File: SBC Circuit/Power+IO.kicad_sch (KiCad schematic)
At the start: 40 parts, among them J1 USB_B, J2 Conn_01x02_Pin, J4 Conn_01x06_Pin, J8 Conn_01x02_Pin, J9 Conn_02x04_Odd_Even, Q1 AOI21357, Q2 AOI21357, U10 FT230XS, U8 LM7805_TO220, U9 LD1117AV33

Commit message: Wire phase done
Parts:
- TP2: value 3V TEST -> 3.3V TEST
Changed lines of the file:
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@@
   (title_block
     (title "POWER & IO")
-    (date "2024-01-26")
-    (rev "0.6")
+    (date "2024-01-31")
+    (rev "0.7")
     (company "LeTourneau University")
     (comment 1 "Richard Homan")
@@
       (effects (font (size 1.27 1.27)) (justify left))
     )
-    (property "Value" "3V TEST" (at 129.54 145.288 0)
-      (effects (font (size 1.27 1.27)) (justify left))
-    )
+    (property "Value" "3.3V TEST" (at 129.54 145.288 0)
+      (effects (font (size 1.27 1.27)) (justify left))
+    )

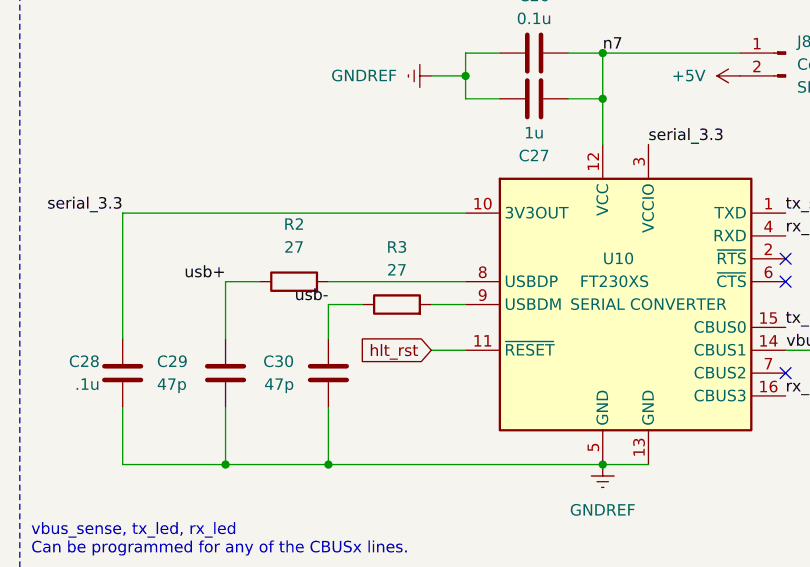
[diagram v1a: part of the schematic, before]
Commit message: All lines connected
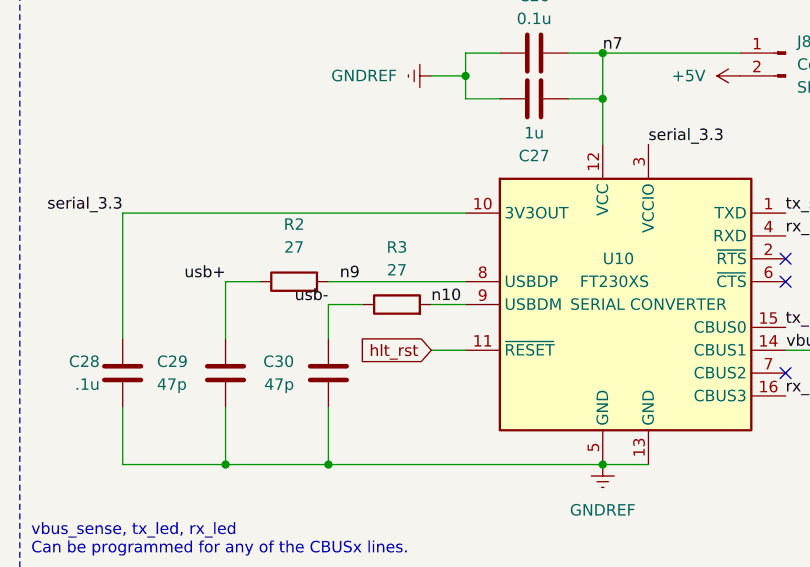
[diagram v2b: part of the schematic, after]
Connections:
- net n9: now reaches R2.2, U10.8 (USBDP)
- net n10: now reaches R3.2, U10.9 (USBDM)
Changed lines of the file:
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@@
     (effects (font (size 1.27 1.27)) (justify right bottom))
+  )
+  (label "n9" (at 54.61 62.23 0) (fields_autoplaced)
+    (effects (font (size 1.27 1.27)) (justify left bottom))
+    (property "Netclass" "signal" (at 54.61 63.5 0)
+      (effects (font (size 1.27 1.27) italic) (justify left) hide)
+    )
   )
   (label "tx_s" (at 250.19 130.81 0) (fields_autoplaced)
@@
     )
   )
+  (label "n10" (at 64.77 64.77 0) (fields_autoplaced)
+    (effects (font (size 1.27 1.27)) (justify left bottom))
+    (property "Netclass" "signal" (at 64.77 66.04 0)
+      (effects (font (size 1.27 1.27) italic) (justify left) hide)
+    )
+  )

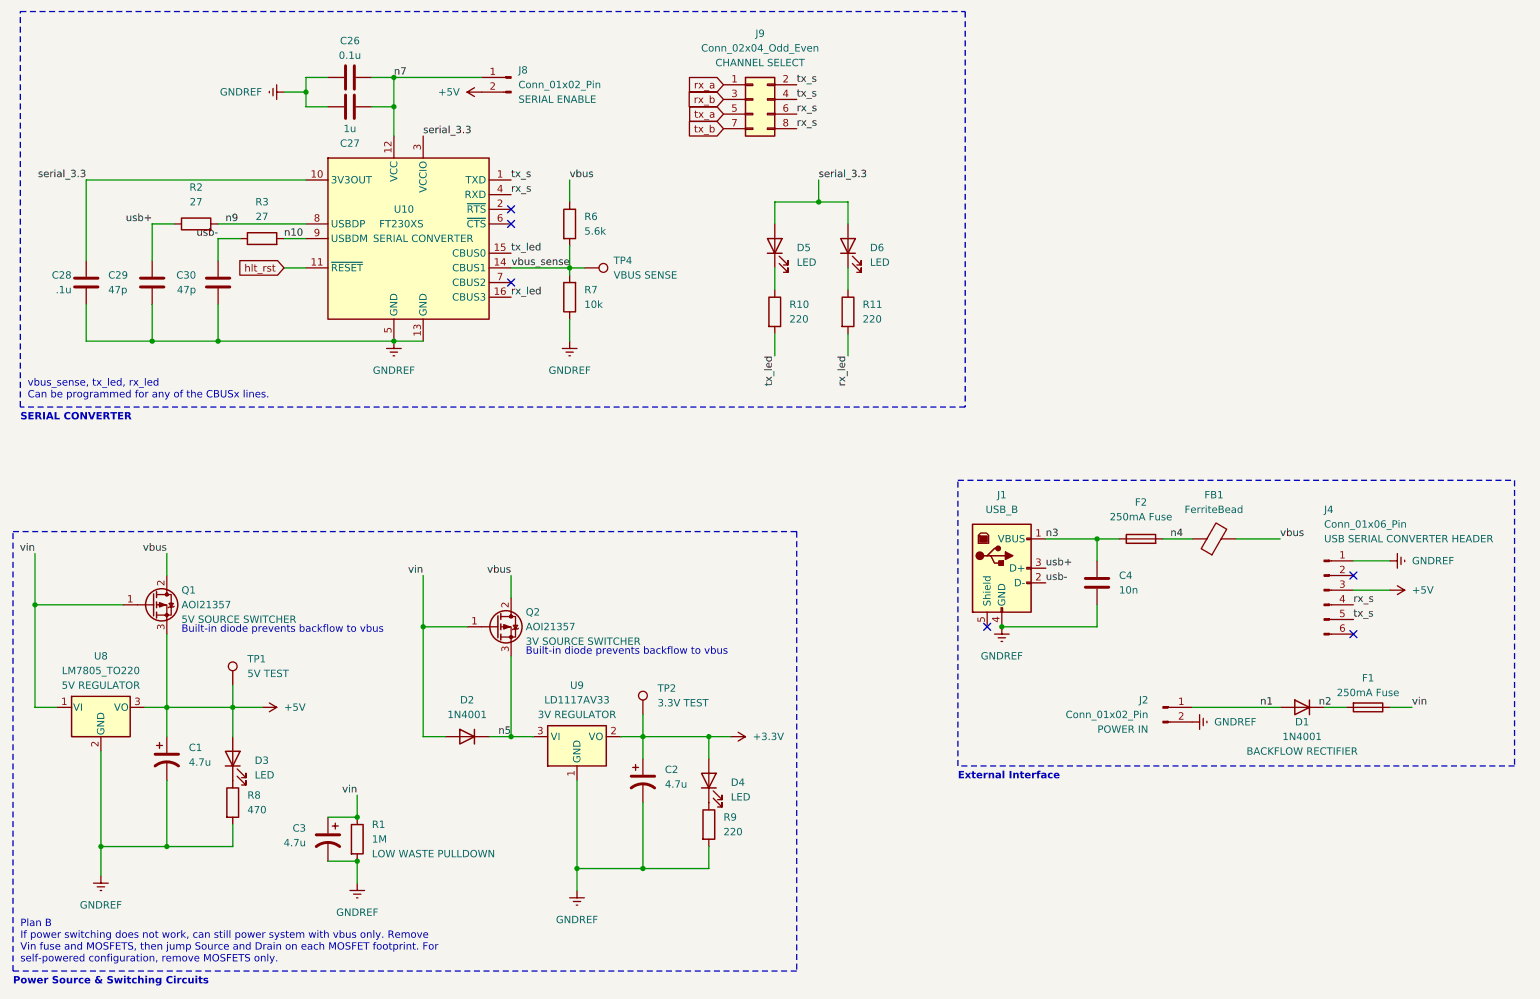
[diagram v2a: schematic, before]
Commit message: Add ground test point
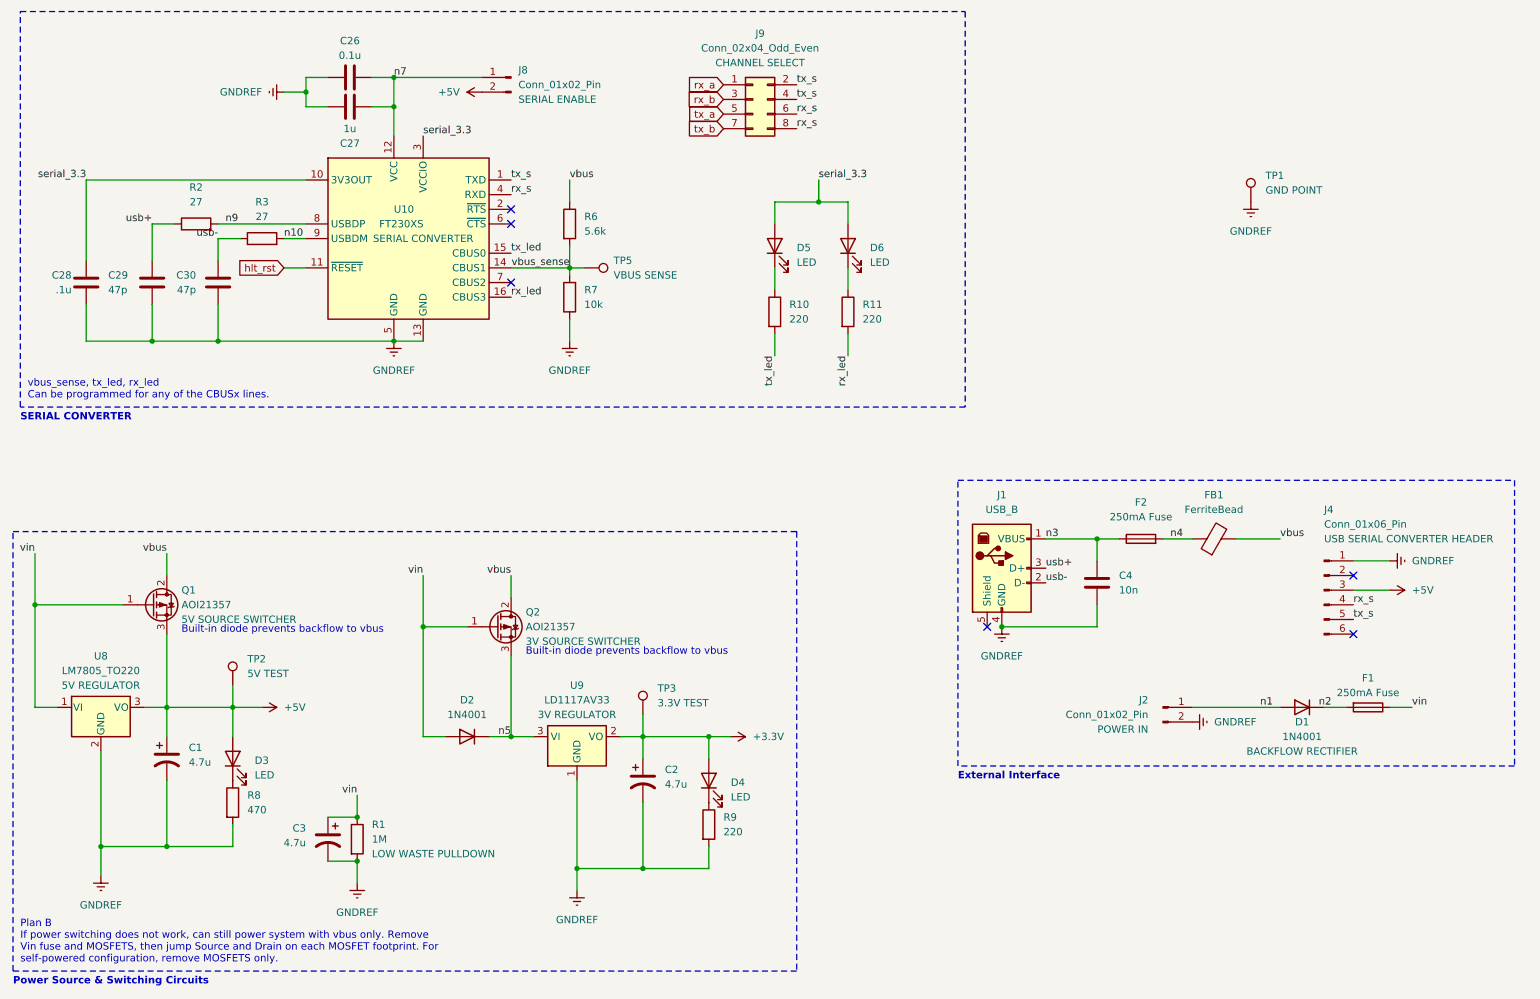
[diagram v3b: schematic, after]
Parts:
- added TP1: GND POINT, TestPoint:TestPoint_Keystone_5000-5004_Miniature, symbol Connector:TestPoint
- renumbered TP1 to TP2, TP2 to TP3, TP4 to TP5
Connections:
- net GNDREF: now also TP1.1

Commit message: Update schematic and PCB for requested changes
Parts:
- renumbered C26 to C30, C27 to C31, C28 to C32, C29 to C33, C30 to C34, R9 to R10, R10 to R11, R11 to R12, R6 to R7, R7 to R8, R8 to R9
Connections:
- net hlt_rst renamed rst
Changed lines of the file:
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@@
   (title_block
     (title "POWER & IO")
-    (date "2024-02-04")
-    (rev "0.8")
+    (date "2024-02-07")
+    (rev "0.9")
     (company "LeTourneau University")
     (comment 1 "Richard Homan")
@@
     )
   )
-  (global_label "hlt_rst" (shape input) (at 64.77 69.85 180) (fields_autoplaced)
+  (global_label "rst" (shape input) (at 64.77 69.85 180) (fields_autoplaced)
     (effects (font (size 1.27 1.27)) (justify right))
     (property "Intersheetrefs" "${INTERSHEET_REFS}" (at 55.7373 69.85 0)
@@
   (symbol (lib_id "Device:C") (at 76.2 36.83 270) (mirror x) (unit 1)
     (in_bom yes) (on_board yes) (dnp no) (fields_autoplaced)
-    (property "Reference" "C26" (at 76.2 30.48 90)
+    (property "Reference" "C30" (at 76.2 30.48 90)
       (effects (font (size 1.27 1.27)))
     )
@@
       (project "SBC Circuit"
         (path "/3db026c4-f98d-4c94-ab2a-d9924b8daebe/8994c9f5-fa11-4f2a-a0bf-cd999f9436d0"
-          (reference "C26") (unit 1)
+          (reference "C30") (unit 1)
         )
       )
@@
   (symbol (lib_id "Device:C") (at 30.48 72.39 0) (mirror y) (unit 1)
     (in_bom yes) (on_board yes) (dnp no)
-    (property "Reference" "C28" (at 27.94 71.12 0)
+    (property "Reference" "C32" (at 27.94 71.12 0)
       (effects (font (size 1.27 1.27)) (justify left))
     )
@@
       (project "SBC Circuit"
         (path "/3db026c4-f98d-4c94-ab2a-d9924b8daebe/8994c9f5-fa11-4f2a-a0bf-cd999f9436d0"
-          (reference "C28") (unit 1)
+          (reference "C32") (unit 1)
         )
       )
@@
   (symbol (lib_id "Device:R") (at 162.56 77.47 0) (unit 1)
     (in_bom yes) (on_board yes) (dnp no) (fields_autoplaced)
-    (property "Reference" "R11" (at 165.1 76.2 0)
+    (property "Reference" "R12" (at 165.1 76.2 0)
       (effects (font (size 1.27 1.27)) (justify left))
     )
@@
       (project "SBC Circuit"
         (path "/3db026c4-f98d-4c94-ab2a-d9924b8daebe/8994c9f5-fa11-4f2a-a0bf-cd999f9436d0"
-          (reference "R11") (unit 1)
+          (reference "R12") (unit 1)
         )
       )
@@
   (symbol (lib_id "Device:R") (at 55.88 162.56 0) (unit 1)
     (in_bom yes) (on_board yes) (dnp no) (fields_autoplaced)
-    (property "Reference" "R8" (at 58.42 161.29 0)
+    (property "Reference" "R9" (at 58.42 161.29 0)
       (effects (font (size 1.27 1.27)) (justify left))
     )
@@
       (project "SBC Circuit"
         (path "/3db026c4-f98d-4c94-ab2a-d9924b8daebe/8994c9f5-fa11-4f2a-a0bf-cd999f9436d0"
+          (reference "R9") (unit 1)
+        )
+      )
+    )
+  )
+  (symbol (lib_id "Device:Fuse") (at 252.73 146.05 270) (unit 1)
+    (in_bom yes) (on_board yes) (dnp no)
+    (property "Reference" "F1" (at 252.73 140.97 90)
+      (effects (font (size 1.27 1.27)))
+    )
+    (property "Value" "250mA Fuse" (at 252.73 143.51 90)
+      (effects (font (size 1.27 1.27)))
+    )
+    (property "Footprint" "Fuse:Fuseholder_Clip-5x20mm_Bel_FC-203-22_Lateral_P17.80x5.00mm_D1.17mm_Horizontal" (at 252.73 144.272 90)
+      (effects (font (size 1.27 1.27)) hide)
+    )
+    (property "Datasheet" "~" (at 252.73 146.05 0)
+      (effects (font (size 1.27 1.27)) hide)
+    )
+    (pin "1")
+    (pin "2")
+    (instances
+      (project "SBC Circuit"
+        (path "/3db026c4-f98d-4c94-ab2a-d9924b8daebe/8994c9f5-fa11-4f2a-a0bf-cd999f9436d0"
+          (reference "F1") (unit 1)
+        )
+      )
+    )
+  )
+  (symbol (lib_id "Device:R") (at 114.3 74.93 180) (unit 1)
+    (in_bom yes) (on_board yes) (dnp no) (fields_autoplaced)
+    (property "Reference" "R8" (at 116.84 73.66 0)
+      (effects (font (size 1.27 1.27)) (justify right))
+    )
+    (property "Value" "10k" (at 116.84 76.2 0)
+      (effects (font (size 1.27 1.27)) (justify right))
+    )
+    (property "Footprint" "Resistor_THT:R_Axial_DIN0204_L3.6mm_D1.6mm_P2.54mm_Vertical" (at 116.078 74.93 90)
+      (effects (font (size 1.27 1.27)) hide)
+    )
+    (property "Datasheet" "~" (at 114.3 74.93 0)
+      (effects (font (size 1.27 1.27)) hide)
+    )
+    (pin "2")
+    (pin "1")
+    (instances
+      (project "SBC Circuit"
+        (path "/3db026c4-f98d-4c94-ab2a-d9924b8daebe/8994c9f5-fa11-4f2a-a0bf-cd999f9436d0"
           (reference "R8") (unit 1)
-        )
-      )
-    )
-  )
-  (symbol (lib_id "Device:Fuse") (at 252.73 146.05 270) (unit 1)
-    (in_bom yes) (on_board yes) (dnp no)
-    (property "Reference" "F1" (at 252.73 140.97 90)
-      (effects (font (size 1.27 1.27)))
-    )
-    (property "Value" "250mA Fuse" (at 252.73 143.51 90)
-      (effects (font (size 1.27 1.27)))
-    )
-    (property "Footprint" "Fuse:Fuseholder_Clip-5x20mm_Bel_FC-203-22_Lateral_P17.80x5.00mm_D1.17mm_Horizontal" (at 252.73 144.272 90)
-      (effects (font (size 1.27 1.27)) hide)
-    )
-    (property "Datasheet" "~" (at 252.73 146.05 0)
-      (effects (font (size 1.27 1.27)) hide)
-    )
-    (pin "1")
-    (pin "2")
-    (instances
-      (project "SBC Circuit"
-        (path "/3db026c4-f98d-4c94-ab2a-d9924b8daebe/8994c9f5-fa11-4f2a-a0bf-cd999f9436d0"
-          (reference "F1") (unit 1)
-        )
-      )
-    )
-  )
-  (symbol (lib_id "Device:R") (at 114.3 74.93 180) (unit 1)
-    (in_bom yes) (on_board yes) (dnp no) (fields_autoplaced)
-    (property "Reference" "R7" (at 116.84 73.66 0)
-      (effects (font (size 1.27 1.27)) (justify right))
-    )
-    (property "Value" "10k" (at 116.84 76.2 0)
-      (effects (font (size 1.27 1.27)) (justify right))
-    )
-    (property "Footprint" "Resistor_THT:R_Axial_DIN0204_L3.6mm_D1.6mm_P2.54mm_Vertical" (at 116.078 74.93 90)
-      (effects (font (size 1.27 1.27)) hide)
-    )
-    (property "Datasheet" "~" (at 114.3 74.93 0)
-      (effects (font (size 1.27 1.27)) hide)
-    )
-    (pin "2")
-    (pin "1")
-    (instances
-      (project "SBC Circuit"
-        (path "/3db026c4-f98d-4c94-ab2a-d9924b8daebe/8994c9f5-fa11-4f2a-a0bf-cd999f9436d0"
-          (reference "R7") (unit 1)
         )
       )
@@
   (symbol (lib_id "Device:R") (at 114.3 62.23 0) (unit 1)
     (in_bom yes) (on_board yes) (dnp no) (fields_autoplaced)
-    (property "Reference" "R6" (at 116.84 60.96 0)
+    (property "Reference" "R7" (at 116.84 60.96 0)
       (effects (font (size 1.27 1.27)) (justify left))
     )
@@
       (project "SBC Circuit"
         (path "/3db026c4-f98d-4c94-ab2a-d9924b8daebe/8994c9f5-fa11-4f2a-a0bf-cd999f9436d0"
-          (reference "R6") (unit 1)
+          (reference "R7") (unit 1)
         )
       )
@@
   (symbol (lib_id "Device:C") (at 53.34 72.39 0) (mirror y) (unit 1)
     (in_bom yes) (on_board yes) (dnp no)
-    (property "Reference" "C30" (at 49.53 71.12 0)
+    (property "Reference" "C34" (at 49.53 71.12 0)
       (effects (font (size 1.27 1.27)) (justify left))
     )
@@
       (project "SBC Circuit"
         (path "/3db026c4-f98d-4c94-ab2a-d9924b8daebe/8994c9f5-fa11-4f2a-a0bf-cd999f9436d0"
-          (reference "C30") (unit 1)
+          (reference "C34") (unit 1)
         )
       )
@@
   (symbol (lib_id "Device:R") (at 149.86 77.47 0) (unit 1)
     (in_bom yes) (on_board yes) (dnp no) (fields_autoplaced)
-    (property "Reference" "R10" (at 152.4 76.2 0)
+    (property "Reference" "R11" (at 152.4 76.2 0)
       (effects (font (size 1.27 1.27)) (justify left))
     )
@@
       (project "SBC Circuit"
         (path "/3db026c4-f98d-4c94-ab2a-d9924b8daebe/8994c9f5-fa11-4f2a-a0bf-cd999f9436d0"
-          (reference "R10") (unit 1)
+          (reference "R11") (unit 1)
         )
       )
@@
   (symbol (lib_id "Device:C") (at 76.2 41.91 270) (unit 1)
     (in_bom yes) (on_board yes) (dnp no)
-    (property "Reference" "C27" (at 76.2 48.26 90)
+    (property "Reference" "C31" (at 76.2 48.26 90)
       (effects (font (size 1.27 1.27)))
     )
@@
       (project "SBC Circuit"
         (path "/3db026c4-f98d-4c94-ab2a-d9924b8daebe/8994c9f5-fa11-4f2a-a0bf-cd999f9436d0"
-          (reference "C27") (unit 1)
+          (reference "C31") (unit 1)
         )
       )
@@
   (symbol (lib_id "Device:R") (at 138.43 166.37 0) (unit 1)
     (in_bom yes) (on_board yes) (dnp no) (fields_autoplaced)
-    (property "Reference" "R9" (at 140.97 165.1 0)
+    (property "Reference" "R10" (at 140.97 165.1 0)
       (effects (font (size 1.27 1.27)) (justify left))
     )
@@
       (project "SBC Circuit"
         (path "/3db026c4-f98d-4c94-ab2a-d9924b8daebe/8994c9f5-fa11-4f2a-a0bf-cd999f9436d0"
-          (reference "R9") (unit 1)
+          (reference "R10") (unit 1)
         )
       )
@@
   (symbol (lib_id "Device:C") (at 41.91 72.39 0) (mirror y) (unit 1)
     (in_bom yes) (on_board yes) (dnp no)
-    (property "Reference" "C29" (at 34.29 71.12 0)
+    (property "Reference" "C33" (at 34.29 71.12 0)
       (effects (font (size 1.27 1.27)) (justify right))
     )
@@
       (project "SBC Circuit"
         (path "/3db026c4-f98d-4c94-ab2a-d9924b8daebe/8994c9f5-fa11-4f2a-a0bf-cd999f9436d0"
-          (reference "C29") (unit 1)
-        )
-      )
+          (reference "C33") (unit 1)
+        )
+      )
